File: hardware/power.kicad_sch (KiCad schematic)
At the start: 29 parts, among them J1 USB4085-GF-A, J2 Batteries, J3 Conn_01x02, J4 Conn_01x02, J5 Conn_01x02, Q1 PMOS, Q2 PMOS, U1 USBLC6-2SC6, U2 TLV76733DGNR

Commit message: HW: Update BOM
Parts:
- D1, D2, D3: value Schottky -> CDBA140LL-HF
- J2: value Batteries -> B2B-PH-K-S
- J3, J4, J5: value Conn_01x02 -> PRPC001DAAN-RC
- Q1, Q2: value PMOS -> FDN338P
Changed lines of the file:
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@@
 	(text "Optional:\nExternal +5V supply"
 		(exclude_from_sim no)
-		(at 154.686 90.17 0)
+		(at 154.94 89.662 0)
 		(effects
 			(font
@@
 			)
 		)
-		(property "Value" "Conn_01x02"
+		(property "Value" "PRPC001DAAN-RC"
 			(at 232.41 41.91 0)
 			(effects
@@
 			)
 		)
-		(property "Value" "Conn_01x02"
+		(property "Value" "PRPC001DAAN-RC"
 			(at 240.03 55.88 0)
 			(effects
@@
 		(dnp no)
 		(property "Reference" "J3"
-			(at 177.8 86.36 0)
+			(at 177.546 86.614 0)
 			(effects
 				(font
@@
 			)
 		)
-		(property "Value" "Conn_01x02"
+		(property "Value" "PRPC001DAAN-RC"
 			(at 173.99 91.44 0)
 			(effects
@@
 			)
 		)
-		(property "Value" "Batteries"
-			(at 104.14 57.15 0)
+		(property "Value" "B2B-PH-K-S"
+			(at 102.616 59.69 0)
 			(effects
 				(font
@@
 				)
 				(justify left)
-				(hide yes)
 			)
 		)
@@
 			)
 		)
-		(property "Value" "PMOS"
+		(property "Value" "FDN338P"
 			(at 157.48 46.482 90)
 			(effects
@@
 			)
 		)
-		(property "Value" "PMOS"
+		(property "Value" "FDN338P"
 			(at 125.73 46.482 90)
 			(effects
@@
 			)
 		)
-		(property "Value" "Schottky"
+		(property "Value" "CDBA140LL-HF"
 			(at 173.0375 45.72 0)
 			(effects
@@
 			)
 		)
-		(property "Value" "Schottky"
+		(property "Value" "CDBA140LL-HF"
 			(at 129.54 53.0225 0)
 			(effects
@@
 			)
 		)
-		(property "Value" "Schottky"
+		(property "Value" "CDBA140LL-HF"
 			(at 173.0375 69.85 0)
 			(effects

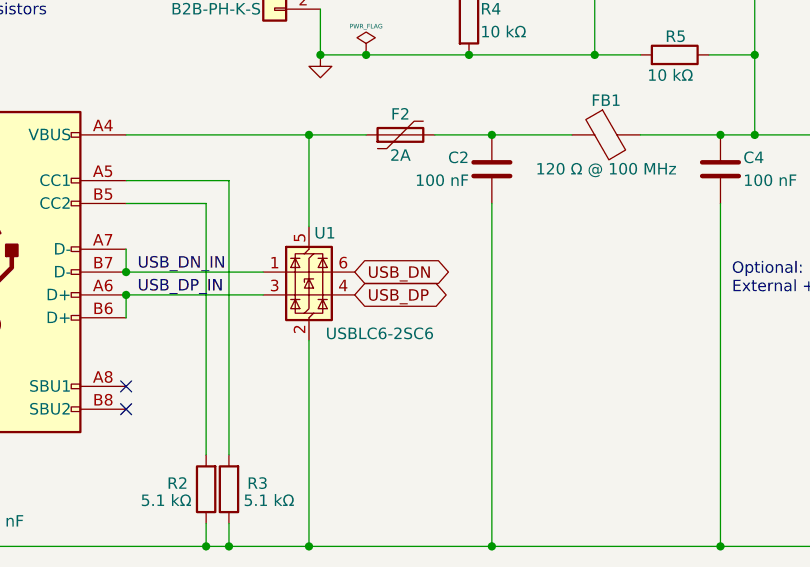
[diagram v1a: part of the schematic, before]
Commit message: HW: Cleanup schematic
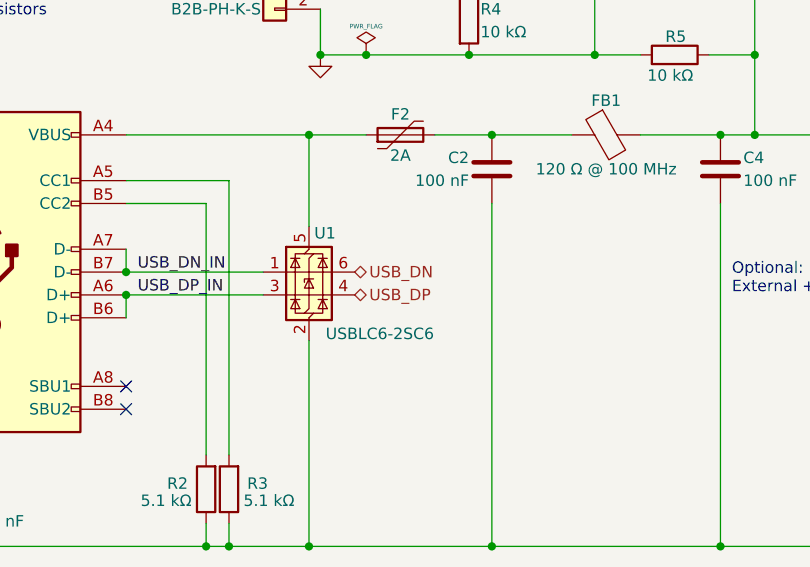
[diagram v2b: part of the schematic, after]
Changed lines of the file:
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@@
 		)
 	)
-	(global_label "USB_DP"
+	(hierarchical_label "USB_DP"
 		(shape bidirectional)
 		(at 113.03 91.44 0)
@@
 			(justify left)
 		)
-		(property "Intersheetrefs" "${INTERSHEET_REFS}"
-			(at 123.6311 91.44 0)
-			(effects
-				(font
-					(size 1.27 1.27)
-				)
-				(justify left)
-				(hide yes)
-			)
-		)
 	)
-	(global_label "USB_DN"
-		(shape bidirectional)
-		(at 113.03 88.9 0)
+	(hierarchical_label "+3.3V"
+		(shape output)
+		(at 243.84 49.53 0)
 		(fields_autoplaced yes)
 		(effects
@@
 			(justify left)
 		)
-		(property "Intersheetrefs" "${INTERSHEET_REFS}"
-			(at 123.6916 88.9 0)
-			(effects
-				(font
-					(size 1.27 1.27)
-				)
-				(justify left)
-				(hide yes)
-			)
-		)
 	)
-	(hierarchical_label "+3.3V"
-		(shape output)
-		(at 243.84 49.53 0)
+	(hierarchical_label "USB_DN"
+		(shape bidirectional)
+		(at 113.03 88.9 0)
 		(fields_autoplaced yes)
 		(effects

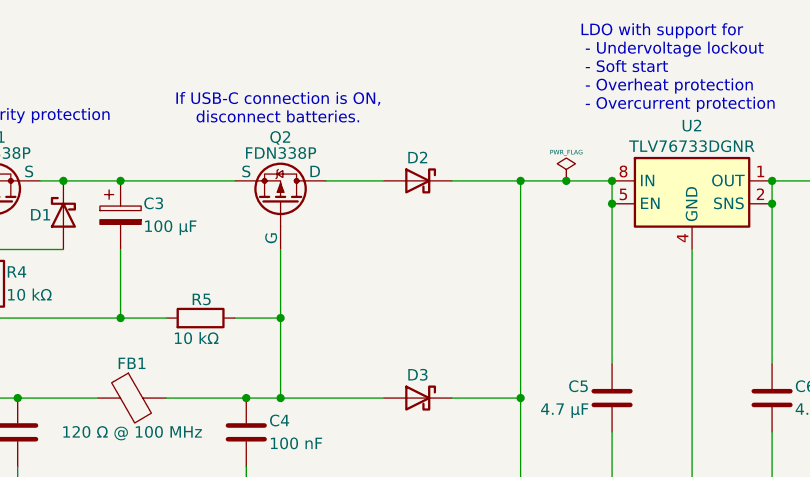
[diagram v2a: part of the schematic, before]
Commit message: HW: Connect +BATT to MCU
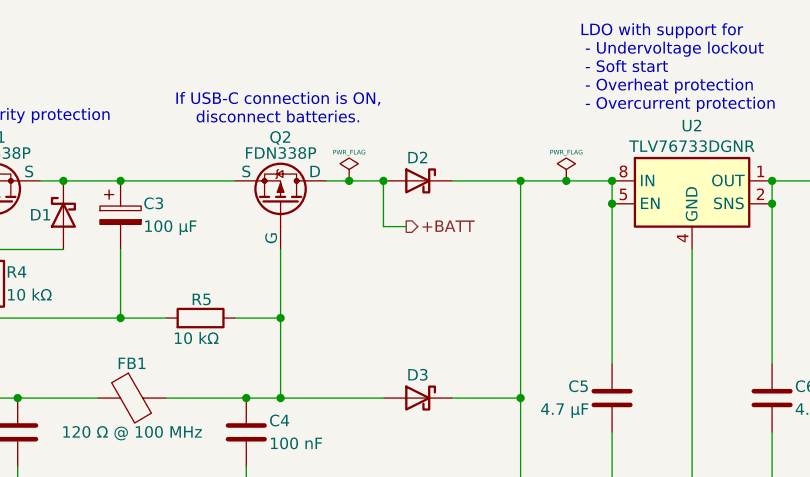
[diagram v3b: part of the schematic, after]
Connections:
- net +BATT: now reaches D2.2 (A), Q2.1 (D)
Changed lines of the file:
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@@
 	(title_block
 		(title "Iida devkit")
-		(date "2024-09-22")
-		(rev "v4.1.0")
+		(date "2024-09-25")
+		(rev "v4.2.0")
 	)
 	(junction
@@
 	)
 	(junction
+		(at 168.91 49.53)
+		(diameter 0)
+		(color 0 0 0 0)
+	)
+	(junction
+		(at 165.1 49.53)
+		(diameter 0)
+		(color 0 0 0 0)
+	)
+	(junction
 		(at 125.73 57.15)
 		(diameter 0)
@@
 	(wire
 		(pts
+			(xy 168.91 54.61) (xy 168.91 49.53)
+		)
+		(stroke
+			(width 0)
+			(type default)
+		)
+	)
+	(wire
+		(pts
 			(xy 157.48 64.77) (xy 157.48 73.66)
 		)
@@
 	(wire
 		(pts
+			(xy 171.45 54.61) (xy 168.91 54.61)
+		)
+		(stroke
+			(width 0)
+			(type default)
+		)
+	)
+	(wire
+		(pts
 			(xy 109.22 64.77) (xy 114.3 64.77)
 		)
@@
 	(wire
 		(pts
+			(xy 165.1 49.53) (xy 168.91 49.53)
+		)
+		(stroke
+			(width 0)
+			(type default)
+		)
+	)
+	(wire
+		(pts
 			(xy 87.63 88.9) (xy 87.63 86.36)
 		)
@@
 	(wire
 		(pts
-			(xy 162.56 49.53) (xy 168.91 49.53)
+			(xy 162.56 49.53) (xy 165.1 49.53)
 		)
 		(stroke
@@
 		)
 	)
+	(hierarchical_label "+BATT"
+		(shape output)
+		(at 171.45 54.61 0)
+		(fields_autoplaced yes)
+		(effects
+			(font
+				(size 1.27 1.27)
+			)
+			(justify left)
+		)
+	)
 	(hierarchical_label "USB_DP"
 		(shape bidirectional)
@@
 		(on_board yes)
 		(dnp no)
-		(property "Reference" "#FLG03"
+		(property "Reference" "#FLG04"
 			(at 242.57 47.625 0)
 			(effects
@@
 			(project "iida_devkit"
 				(path "/b12a6e25-97fb-4aba-bc96-af8db389bb9a/8a51e004-740e-440f-9bfb-b035bcbeb0d2"
-					(reference "#FLG03")
+					(reference "#FLG04")
 					(unit 1)
 				)
@@
 	)
 	(symbol
+		(lib_id "power:PWR_FLAG")
+		(at 165.1 49.53 0)
+		(mirror y)
+		(unit 1)
+		(exclude_from_sim no)
+		(in_bom yes)
+		(on_board yes)
+		(dnp no)
+		(property "Reference" "#FLG02"
+			(at 165.1 47.625 0)
+			(effects
+				(font
+					(size 1.27 1.27)
+				)
+				(hide yes)
+			)
+		)
+		(property "Value" "PWR_FLAG"
+			(at 165.1 46.355 0)
+			(effects
+				(font
+					(size 0.5 0.5)
+				)
+			)
+		)
+		(property "Footprint" ""
+			(at 165.1 49.53 0)
+			(effects
+				(font
+					(size 1.27 1.27)
+				)
+				(hide yes)
+			)
+		)
+		(property "Datasheet" "~"
+			(at 165.1 49.53 0)
+			(effects
+				(font
+					(size 1.27 1.27)
+				)
+				(hide yes)
+			)
+		)
+		(property "Description" "Special symbol for telling ERC where power comes from"
+			(at 165.1 49.53 0)
+			(effects
+				(font
+					(size 1.27 1.27)
+				)
+				(hide yes)
+			)
+		)
+		(pin "1"
+		)
+		(instances
+			(project "iida_devkit"
+				(path "/b12a6e25-97fb-4aba-bc96-af8db389bb9a/8a51e004-740e-440f-9bfb-b035bcbeb0d2"
+					(reference "#FLG02")
+					(unit 1)
+				)
+			)
+		)
+	)
+	(symbol
 		(lib_id "Device:C")
 		(at 153.67 77.47 0)
@@
 		(on_board yes)
 		(dnp no)
-		(property "Reference" "#FLG02"
+		(property "Reference" "#FLG03"
 			(at 189.23 47.625 0)
 			(effects
@@
 			(project "iida_devkit"
 				(path "/b12a6e25-97fb-4aba-bc96-af8db389bb9a/8a51e004-740e-440f-9bfb-b035bcbeb0d2"
-					(reference "#FLG02")
+					(reference "#FLG03")
 					(unit 1)
 				)

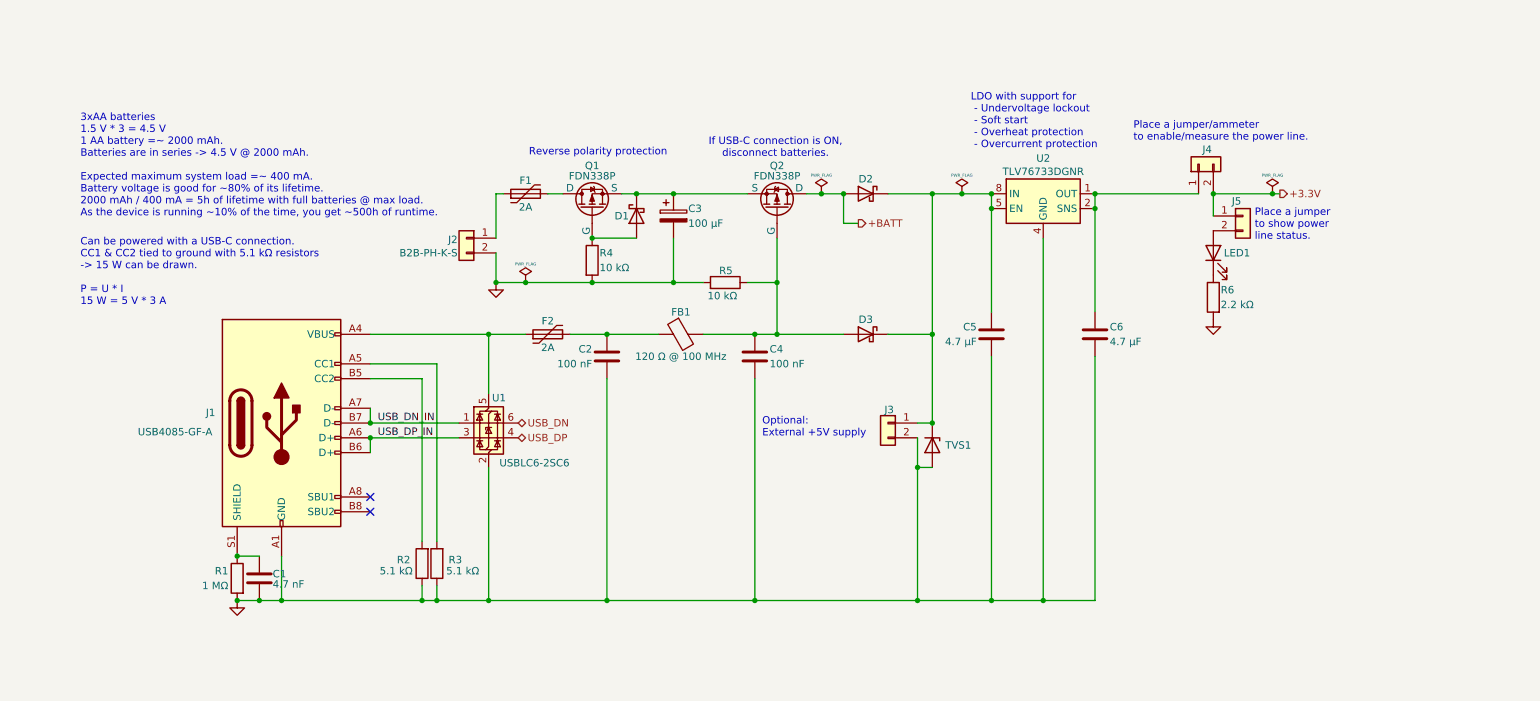
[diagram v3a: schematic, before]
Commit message: HW: Improve thermals, silkscreen and schematic
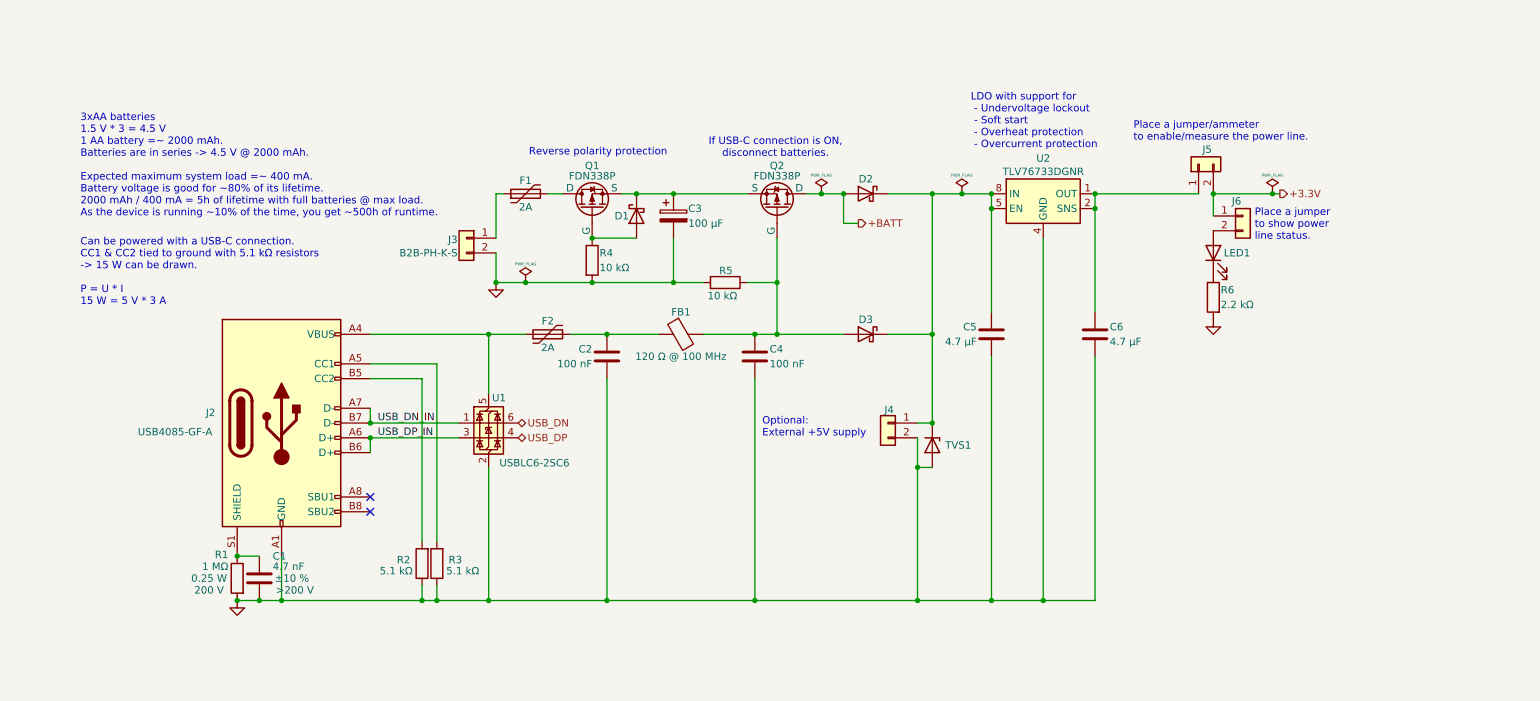
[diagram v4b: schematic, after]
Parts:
- C1: footprint perfect_footprints:0402_1005_perfect -> Capacitor_SMD:C_0805_2012Metric; Digi-Key Part Number 490-3885-1-ND -> 732-12165-1-ND; Manufacturer Murata Electronics -> Würth Elektronik; Manufacturer Part Number GRM155R72A472KA01D -> 885342207009; Tolerance (none) -> ±10 %; Voltage rating (none) -> >200 V
- R1: footprint Resistor_SMD:R_0805_2012Metric -> Resistor_SMD:R_1206_3216Metric; Digi-Key Part Number 311-1.0MARCT-ND -> RHM1.0MPCT-ND; Manufacturer YAGEO -> Rohm Semiconductor; Manufacturer Part Number RC0805JR-071ML -> KTR18EZPJ105; Power rating (none) -> 0.25 W; Working voltage (none) -> 200 V
- renumbered J1 to J2, J2 to J3, J3 to J4, J4 to J5, J5 to J6
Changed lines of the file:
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@@
 		(dnp no)
 		(fields_autoplaced yes)
-		(property "Reference" "#PWR03"
+		(property "Reference" "#PWR04"
 			(at 109.22 71.12 0)
 			(effects
@@
 			(project "iida_devkit"
 				(path "/b12a6e25-97fb-4aba-bc96-af8db389bb9a/8a51e004-740e-440f-9bfb-b035bcbeb0d2"
-					(reference "#PWR03")
+					(reference "#PWR04")
 					(unit 1)
 				)
@@
 		(dnp no)
 		(property "Reference" "C1"
-			(at 70.866 114.808 0)
+			(at 70.866 111.76 0)
 			(effects
 				(font
@@
 		)
 		(property "Value" "4.7 nF"
-			(at 70.866 116.586 0)
+			(at 70.866 113.538 0)
 			(effects
 				(font
@@
 			)
 		)
-		(property "Footprint" "perfect_footprints:0402_1005_perfect"
+		(property "Footprint" "Capacitor_SMD:C_0805_2012Metric"
 			(at 69.5452 119.38 0)
 			(effects
@@
 			)
 		)
-		(property "Manufacturer" "Murata Electronics"
+		(property "Manufacturer" "Würth Elektronik"
 			(at 68.58 115.57 0)
 			(effects
@@
 			)
 		)
-		(property "Manufacturer Part Number" "GRM155R72A472KA01D"
+		(property "Manufacturer Part Number" "885342207009"
 			(at 68.58 115.57 0)
 			(effects
@@
 			)
 		)
-		(property "Digi-Key Part Number" "490-3885-1-ND"
+		(property "Digi-Key Part Number" "732-12165-1-ND"
 			(at 68.58 115.57 0)
 			(effects
@@
 			)
 		)
+		(property "Voltage rating" ">200 V"
+			(at 74.676 117.602 0)
+			(effects
+				(font
+					(size 1.27 1.27)
+				)
+			)
+		)
+		(property "Tolerance" "±10 %"
+			(at 74.168 115.57 0)
+			(effects
+				(font
+					(size 1.27 1.27)
+				)
+			)
+		)
 		(pin "2"
 		)
@@
 		(on_board yes)
 		(dnp no)
-		(property "Reference" "J4"
+		(property "Reference" "J5"
 			(at 232.156 41.91 90)
 			(effects
@@
 			(project "iida_devkit"
 				(path "/b12a6e25-97fb-4aba-bc96-af8db389bb9a/8a51e004-740e-440f-9bfb-b035bcbeb0d2"
-					(reference "J4")
+					(reference "J5")
 					(unit 1)
 				)
@@
 		(on_board yes)
 		(dnp no)
-		(property "Reference" "J5"
+		(property "Reference" "J6"
 			(at 235.585 50.8 0)
 			(effects
@@
 			(project "iida_devkit"
 				(path "/b12a6e25-97fb-4aba-bc96-af8db389bb9a/8a51e004-740e-440f-9bfb-b035bcbeb0d2"
-					(reference "J5")
+					(reference "J6")
 					(unit 1)
 				)
@@
 		(dnp no)
 		(property "Reference" "R1"
-			(at 63.246 114.3 0)
+			(at 63.246 111.506 0)
 			(effects
 				(font
@@
 		)
 		(property "Value" "1 MΩ"
-			(at 63.246 116.84 0)
+			(at 63.246 113.538 0)
 			(effects
 				(font
@@
 			)
 		)
-		(property "Footprint" "Resistor_SMD:R_0805_2012Metric"
+		(property "Footprint" "Resistor_SMD:R_1206_3216Metric"
 			(at 66.548 115.57 90)
 			(effects
@@
 			)
 		)
-		(property "Manufacturer" "YAGEO"
+		(property "Manufacturer" "Rohm Semiconductor"
 			(at 64.77 115.57 0)
 			(effects
@@
 			)
 		)
-		(property "Manufacturer Part Number" "RC0805JR-071ML"
+		(property "Manufacturer Part Number" "KTR18EZPJ105"
 			(at 64.77 115.57 0)
 			(effects
@@
 			)
 		)
-		(property "Digi-Key Part Number" "311-1.0MARCT-ND"
+		(property "Digi-Key Part Number" "RHM1.0MPCT-ND"
 			(at 64.77 115.57 0)
 			(effects
@@
 			)
 		)
+		(property "Power rating" "0.25 W"
+			(at 59.944 115.57 0)
+			(effects
+				(font
+					(size 1.27 1.27)
+				)
+			)
+		)
+		(property "Working voltage" "200 V"
+			(at 59.944 117.602 0)
+			(effects
+				(font
+					(size 1.27 1.27)
+				)
+			)
+		)
 		(pin "1"
 		)
@@
 		(on_board yes)
 		(dnp no)
-		(property "Reference" "J1"
+		(property "Reference" "J2"
 			(at 60.198 87.122 0)
 			(effects
@@
 			(project ""
 				(path "/b12a6e25-97fb-4aba-bc96-af8db389bb9a/8a51e004-740e-440f-9bfb-b035bcbeb0d2"
-					(reference "J1")
+					(reference "J2")
 					(unit 1)
 				)
@@
 		(on_board yes)
 		(dnp no)
-		(property "Reference" "J3"
+		(property "Reference" "J4"
 			(at 177.546 86.614 0)
 			(effects
@@
 			(project "iida_devkit"
 				(path "/b12a6e25-97fb-4aba-bc96-af8db389bb9a/8a51e004-740e-440f-9bfb-b035bcbeb0d2"
-					(reference "J3")
+					(reference "J4")
 					(unit 1)
 				)
@@
 		(on_board yes)
 		(dnp no)
-		(property "Reference" "J2"
+		(property "Reference" "J3"
 			(at 102.616 57.404 0)
 			(effects
@@
 			(project "iida_devkit"
 				(path "/b12a6e25-97fb-4aba-bc96-af8db389bb9a/8a51e004-740e-440f-9bfb-b035bcbeb0d2"
-					(reference "J2")
+					(reference "J3")
 					(unit 1)
 				)
@@
 		(dnp no)
 		(fields_autoplaced yes)
-		(property "Reference" "#PWR02"
+		(property "Reference" "#PWR03"
 			(at 64.77 125.73 0)
 			(effects
@@
 			(project "iida_devkit"
 				(path "/b12a6e25-97fb-4aba-bc96-af8db389bb9a/8a51e004-740e-440f-9bfb-b035bcbeb0d2"
-					(reference "#PWR02")
+					(reference "#PWR03")
 					(unit 1)
 				)
@@
 		(dnp no)
 		(fields_autoplaced yes)
-		(property "Reference" "#PWR04"
+		(property "Reference" "#PWR05"
 			(at 232.41 77.47 0)
 			(effects
@@
 			(project "iida_devkit"
 				(path "/b12a6e25-97fb-4aba-bc96-af8db389bb9a/8a51e004-740e-440f-9bfb-b035bcbeb0d2"
-					(reference "#PWR04")
+					(reference "#PWR05")
 					(unit 1)
 				)
